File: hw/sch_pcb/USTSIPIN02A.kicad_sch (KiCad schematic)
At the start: 63 parts, among them M1 HOLE, M2 HOLE, M3 HOLE, M4 HOLE, M8 BMI-S-204-F, Q1 2SK2394-6, U1 OPA2314, U2 OPA2314, U3 ISL21080DIH312Z-TK 1V25, U4 TS7211, U5 TS5A4594

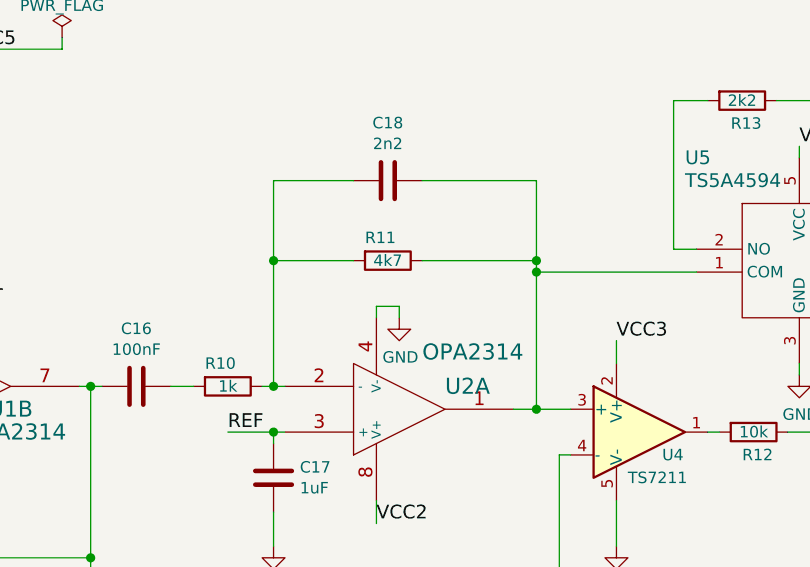
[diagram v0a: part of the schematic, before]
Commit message: Change crystal frequency to 8 MHz to solve #12
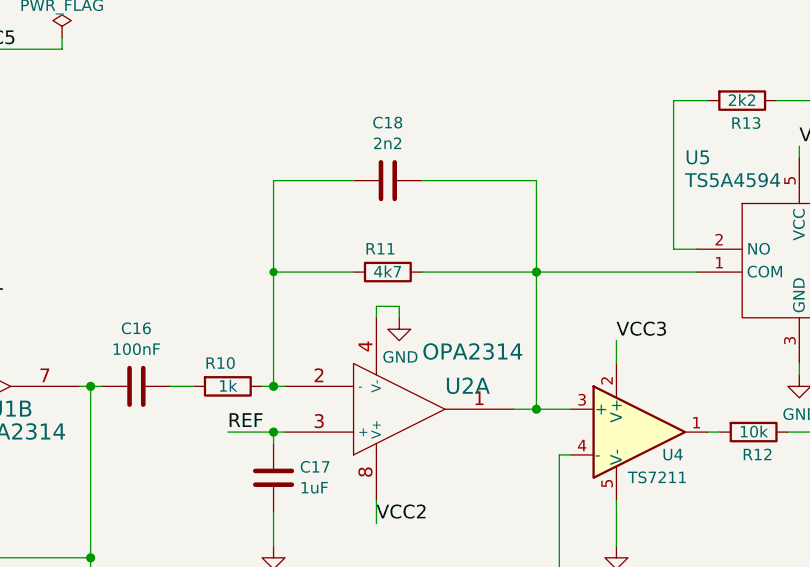
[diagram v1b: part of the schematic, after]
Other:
- moved on the sheet: R11
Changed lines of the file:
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@@
   (junction (at 85.09 36.83) (diameter 1.016) (color 0 0 0 0)
   )
-  (junction (at 171.45 111.76) (diameter 1.016) (color 0 0 0 0)
-  )
   (junction (at 96.52 20.32) (diameter 1.016) (color 0 0 0 0)
   )
@@
   (junction (at 171.45 113.03) (diameter 1.016) (color 0 0 0 0)
   )
+  (junction (at 142.24 113.03) (diameter 0) (color 0 0 0 0)
+  )
   (junction (at 48.26 110.49) (diameter 1.016) (color 0 0 0 0)
   )
@@
   (junction (at 30.48 97.79) (diameter 0) (color 0 0 0 0)
   )
-  (junction (at 142.24 111.76) (diameter 1.016) (color 0 0 0 0)
-  )
   (junction (at 44.45 125.73) (diameter 1.016) (color 0 0 0 0)
   )
@@
     (stroke (width 0) (type solid) (color 0 0 0 0))
   )
-  (wire (pts (xy 158.75 111.76) (xy 171.45 111.76))
+  (wire (pts (xy 158.75 113.03) (xy 171.45 113.03))
     (stroke (width 0) (type solid) (color 0 0 0 0))
   )
@@
     (stroke (width 0) (type default) (color 0 0 0 0))
   )
-  (wire (pts (xy 171.45 102.87) (xy 171.45 111.76))
-    (stroke (width 0) (type solid) (color 0 0 0 0))
-  )
   (wire (pts (xy 58.42 133.35) (xy 60.96 133.35))
     (stroke (width 0) (type solid) (color 0 0 0 0))
@@
     (stroke (width 0) (type solid) (color 0 0 0 0))
   )
-  (wire (pts (xy 151.13 111.76) (xy 142.24 111.76))
+  (wire (pts (xy 151.13 113.03) (xy 142.24 113.03))
     (stroke (width 0) (type solid) (color 0 0 0 0))
   )
@@
     (stroke (width 0) (type solid) (color 0 0 0 0))
   )
-  (wire (pts (xy 142.24 111.76) (xy 142.24 102.87))
+  (wire (pts (xy 142.24 102.87) (xy 142.24 113.03))
     (stroke (width 0) (type solid) (color 0 0 0 0))
   )
@@
     (stroke (width 0) (type default) (color 0 0 0 0))
   )
-  (wire (pts (xy 142.24 125.73) (xy 142.24 111.76))
+  (wire (pts (xy 142.24 125.73) (xy 142.24 113.03))
     (stroke (width 0) (type solid) (color 0 0 0 0))
   )
@@
     (stroke (width 0) (type solid) (color 0 0 0 0))
   )
-  (wire (pts (xy 171.45 111.76) (xy 171.45 113.03))
+  (wire (pts (xy 171.45 102.87) (xy 171.45 113.03))
     (stroke (width 0) (type solid) (color 0 0 0 0))
   )
@@
     (pin "2")
   )
-  (symbol (lib_id "Device:R") (at 154.94 111.76 270) (unit 1)
+  (symbol (lib_id "Device:R") (at 154.94 113.03 270) (unit 1)
     (in_bom yes) (on_board yes)
-    (property "Reference" "R11" (id 0) (at 152.4 109.22 90)
+    (property "Reference" "R11" (id 0) (at 152.4 110.49 90)
       (effects (font (size 1.27 1.27)) (justify left))
     )
-    (property "Value" "4k7" (id 1) (at 154.94 111.76 90))
-    (property "Footprint" "Resistor_SMD:R_0603_1608Metric" (id 2) (at 154.94 109.982 90)
+    (property "Value" "4k7" (id 1) (at 154.94 113.03 90))
+    (property "Footprint" "Resistor_SMD:R_0603_1608Metric" (id 2) (at 154.94 111.252 90)
       (effects (font (size 1.27 1.27)) hide)
     )
-    (property "Datasheet" "~" (id 3) (at 154.94 111.76 0)
+    (property "Datasheet" "~" (id 3) (at 154.94 113.03 0)
       (effects (font (size 1.27 1.27)) hide)
     )
-    (property "UST_ID" "5c70984512875079b91f8960" (id 4) (at 154.94 111.76 0)
+    (property "UST_ID" "5c70984512875079b91f8960" (id 4) (at 154.94 113.03 0)
       (effects (font (size 1.27 1.27)) hide)
     )
@@
     )
     (path "/00000000-0000-0000-0000-00005c4aedd8/00000000-0000-0000-0000-00005b257330"
-      (reference "Y1") (unit 1) (value "16MHz") (footprint "Mlab_XTAL:Crystal_HC49-4H_Vertical")
+      (reference "Y1") (unit 1) (value "8 MHz") (footprint "Mlab_XTAL:Crystal_HC49-4H_Vertical")
     )
     (path "/00000000-0000-0000-0000-00005c4aedd8/00000000-0000-0000-0000-00005b36b778"

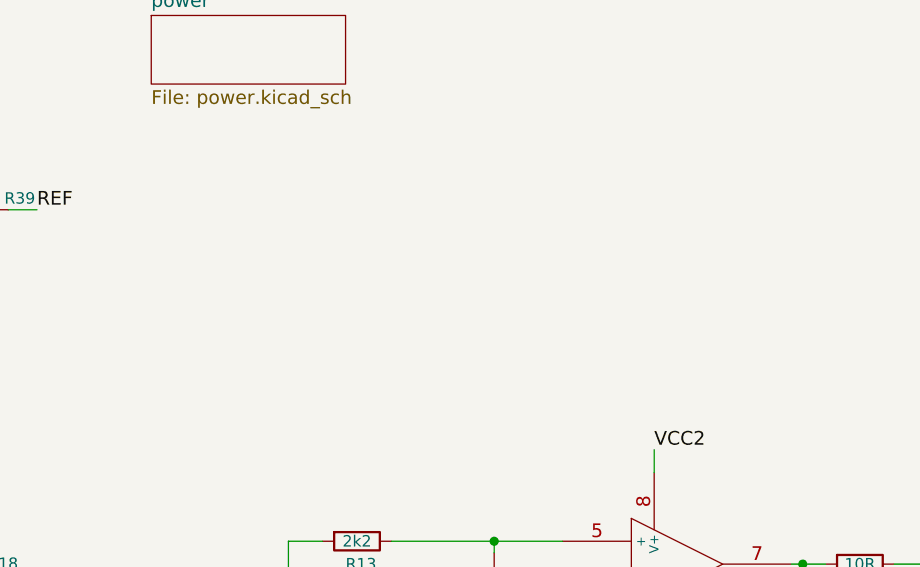
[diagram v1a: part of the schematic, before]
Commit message: Update PCB from schematics.
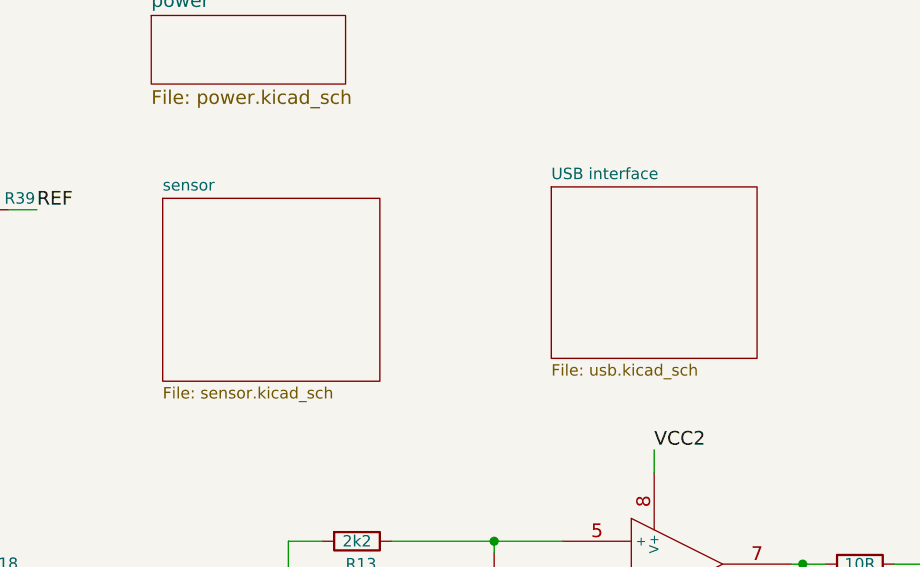
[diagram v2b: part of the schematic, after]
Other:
- added sheet USB interface (usb.kicad_sch)
- added sheet sensor (sensor.kicad_sch)
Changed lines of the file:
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@@
+    )
+  )
+  (sheet (at 215.9 54.61) (size 22.86 19.05) (fields_autoplaced)
+    (stroke (width 0.1524) (type solid) (color 0 0 0 0))
+    (fill (color 0 0 0 0.0000))
+    (property "Sheet name" "USB interface" (id 0) (at 215.9 53.8984 0)
+      (effects (font (size 1.27 1.27)) (justify left bottom))
+    )
+    (property "Sheet file" "usb.kicad_sch" (id 1) (at 215.9 74.2446 0)
+      (effects (font (size 1.27 1.27)) (justify left top))
+    )
+  )
+  (sheet (at 172.72 55.88) (size 24.13 20.32) (fields_autoplaced)
+    (stroke (width 0.1524) (type solid) (color 0 0 0 0))
+    (fill (color 0 0 0 0.0000))
+    (property "Sheet name" "sensor" (id 0) (at 172.72 55.1684 0)
+      (effects (font (size 1.27 1.27)) (justify left bottom))
+    )
+    (property "Sheet file" "sensor.kicad_sch" (id 1) (at 172.72 76.7846 0)
+      (effects (font (size 1.27 1.27)) (justify left top))
     )
   )
@@
     (path "/00000000-0000-0000-0000-00005c4aedd8" (page "2"))
     (path "/00000000-0000-0000-0000-00005c69bcb4" (page "3"))
+    (path "/df946b97-ee48-4dc9-bb94-44edab77d662" (page "4"))
+    (path "/19d1d659-a959-4bd5-b510-08a4dbcee178" (page "5"))
   )
   (symbol_instances
@@
       (reference "#FLG0109") (unit 1) (value "PWR_FLAG") (footprint "")
     )
+    (path "/00000000-0000-0000-0000-00005c69bcb4/4ec5e526-6220-41d1-9225-2c87bd89c49e"
+      (reference "#FLG0110") (unit 1) (value "PWR_FLAG") (footprint "")
+    )
     (path "/00000000-0000-0000-0000-00005c69bcb4/c9236cab-2bb1-4aa1-a5cb-30113553a821"
       (reference "#FLG0110") (unit 1) (value "PWR_FLAG") (footprint "")
     )
-    (path "/00000000-0000-0000-0000-00005c69bcb4/4ec5e526-6220-41d1-9225-2c87bd89c49e"
-      (reference "#FLG?") (unit 1) (value "PWR_FLAG") (footprint "")
-    )
     (path "/00000000-0000-0000-0000-00005c4aedd8/4e0ca0d2-2b6d-45f5-ad3e-54509fad15ee"

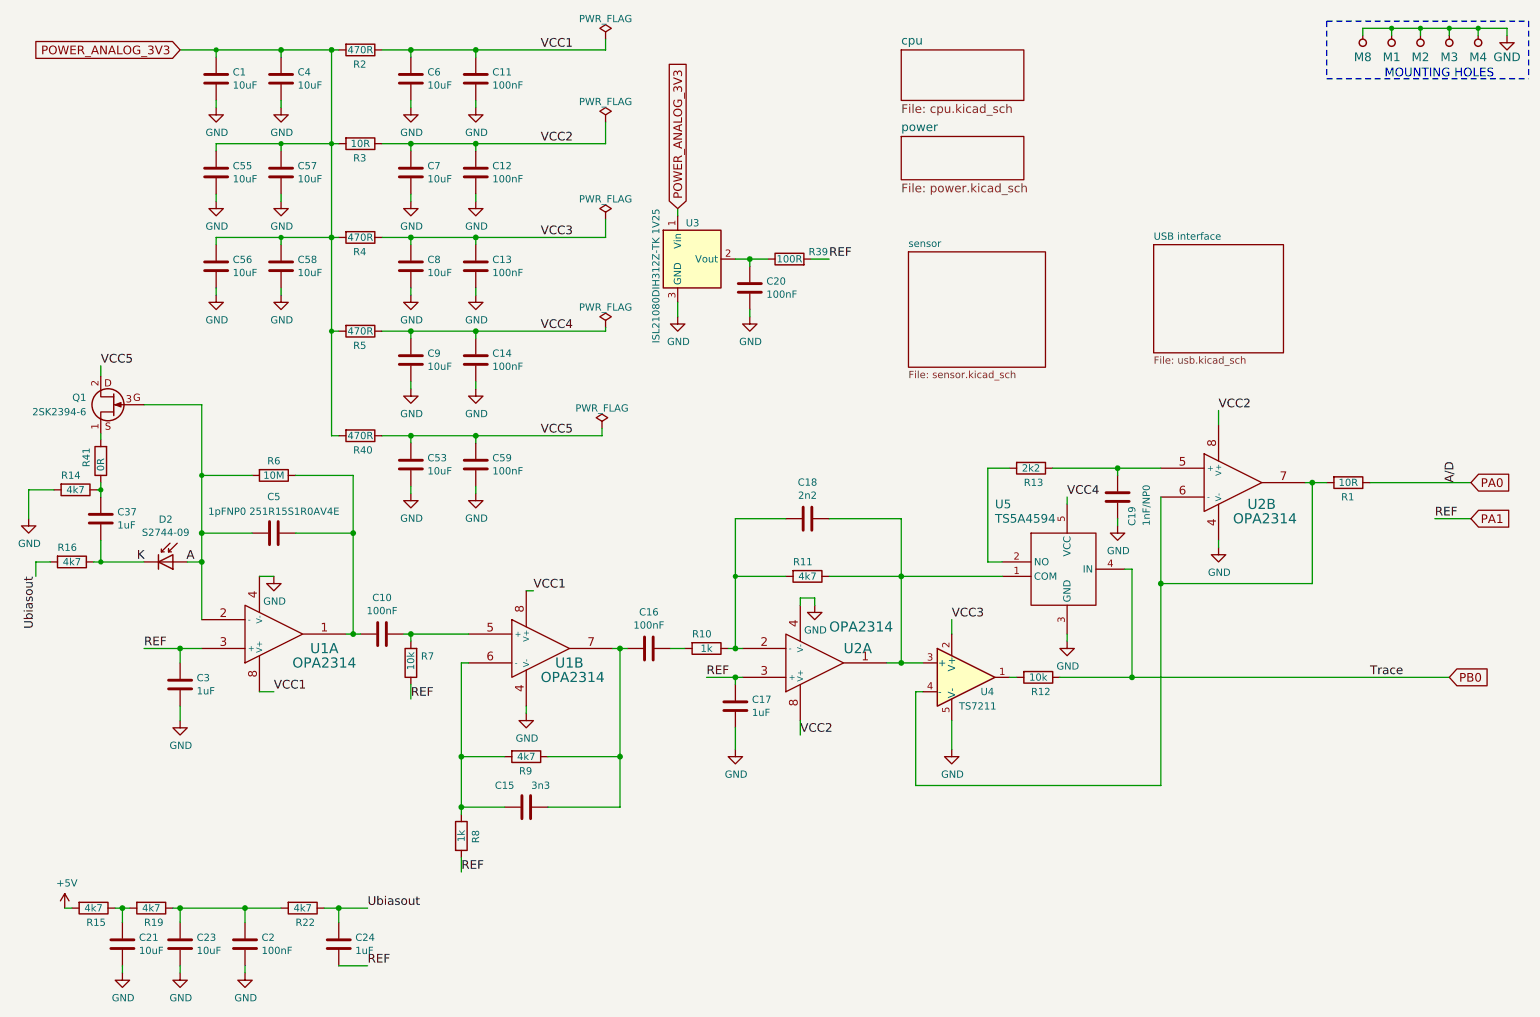
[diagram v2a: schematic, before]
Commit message: Schematics structure change.
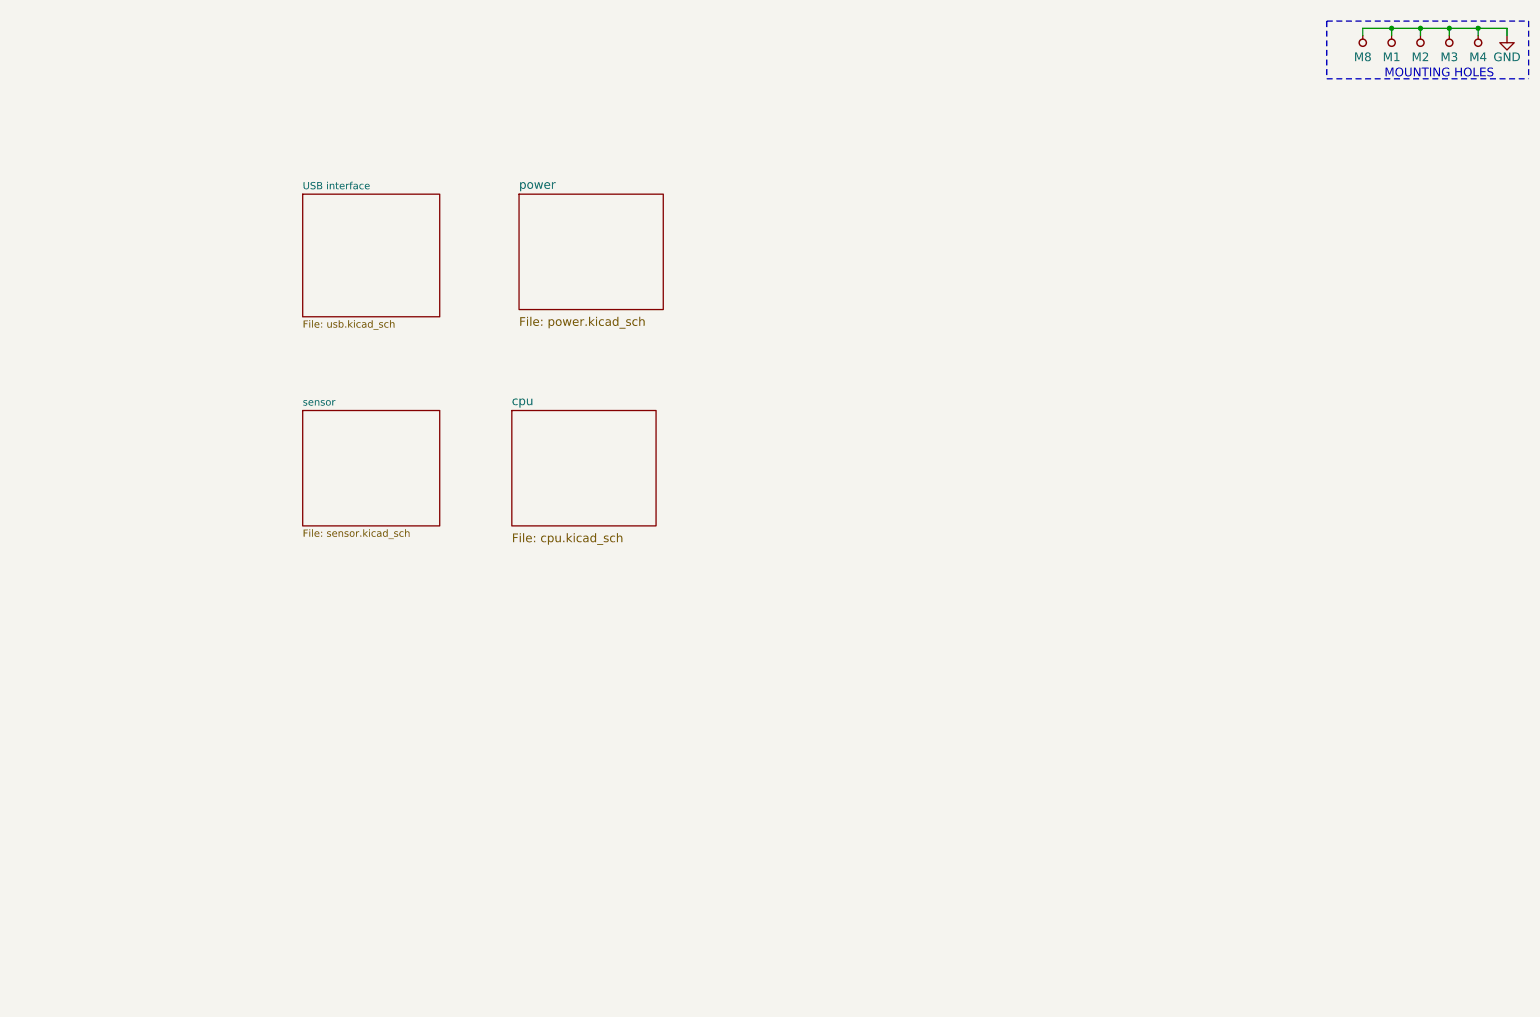
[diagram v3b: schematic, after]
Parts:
- removed C1, C21, C23, C4, C53, C55, C56, C57, C58, C6, C7, C8, C9: 10uF, Capacitor_SMD:C_0603_1608Metric, symbol Device:C
- removed C10, C11, C12, C13, C14, C16, C2, C20, C59: 100nF, Capacitor_SMD:C_0603_1608Metric, symbol Device:C
- removed C15: 3n3, Capacitor_SMD:C_0603_1608Metric, symbol Device:C
- removed C17, C24, C3, C37: 1uF, Capacitor_SMD:C_0603_1608Metric, symbol Device:C
- removed C18: 2n2, Capacitor_SMD:C_0603_1608Metric, symbol Device:C
- removed C19: 1nF/NP0, Capacitor_SMD:C_0805_2012Metric, symbol Device:C
- removed C5: 1pFNP0 251R15S1R0AV4E, Capacitor_SMD:C_0805_2012Metric, symbol Device:C
- removed D2: S2744-09, Mlab_D:HAMAMATSU_S2744-09, symbol Device:D_Photo
- removed Q1: 2SK2394-6, Package_TO_SOT_SMD:SOT-23, symbol MLAB_T:Q_NJFET_SDG
- removed R1, R3: 10R, Resistor_SMD:R_0603_1608Metric, symbol Device:R
- removed R10, R8: 1k, Resistor_SMD:R_0603_1608Metric, symbol Device:R
- removed R11, R14, R15, R16, R19, R22, R9: 4k7, Resistor_SMD:R_0603_1608Metric, symbol Device:R
- removed R12, R7: 10k, Resistor_SMD:R_0603_1608Metric, symbol Device:R
- removed R13: 2k2, Resistor_SMD:R_0603_1608Metric, symbol Device:R
- removed R2, R4, R40, R5: 470R, Resistor_SMD:R_0603_1608Metric, symbol Device:R
- removed R39: 100R, Resistor_SMD:R_0603_1608Metric, symbol SPACEDOS02A_PCB01A-rescue:R-device-DATALOGGER01A-rescue-CCP2019V01A-rescue-SPAC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
- removed R41: 0R, Resistor_SMD:R_0603_1608Metric, symbol Device:R
- removed R6: 10M, Resistor_SMD:R_0603_1608Metric, symbol Device:R
- removed U1, U2: OPA2314, Package_SO:SOIC-8_3.9x4.9mm_P1.27mm, symbol MLAB_IO:AD8692
- removed U3: ISL21080DIH312Z-TK 1V25, Package_TO_SOT_SMD:SOT-23, symbol Reference_Voltage:ISL21070CIH320Z-TK
- removed U4: TS7211, Package_TO_SOT_SMD:SOT-23-5_HandSoldering, symbol Amplifier_Operational:OP179GRT
- removed U5: TS5A4594, Package_TO_SOT_SMD:SOT-23-5_HandSoldering, symbol MLAB_IO:TS5A4594

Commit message: Schematics cleanup of power symbols and routing.
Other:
- sheet USB interface ports: added VUSB; removed none
- sheet power ports: added VUSB; removed none
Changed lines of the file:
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@@
     (stroke (width 0) (type solid) (color 0 0 0 0))
+  )
+  (wire (pts (xy 90.17 50.8) (xy 104.14 50.8))
+    (stroke (width 0) (type default) (color 0 0 0 0))
   )
   (wire (pts (xy 262.89 17.78) (xy 262.89 16.51))
@@
       (effects (font (size 1.524 1.524)) (justify left top))
     )
+    (pin "VUSB" input (at 104.14 50.8 180)
+      (effects (font (size 1.524 1.524)) (justify left))
+    )
   )
   (sheet (at 66.04 45.72) (size 24.13 21.59) (fields_autoplaced)
@@
       (effects (font (size 1.27 1.27)) (justify left top))
     )
+    (pin "VUSB" input (at 90.17 50.8 0)
+      (effects (font (size 1.524 1.524)) (justify right))
+    )
   )
